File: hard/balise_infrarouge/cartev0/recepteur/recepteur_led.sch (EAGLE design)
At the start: 112 parts, among them IC2 7805DT, IC3 4051D, IC4 4051D, IC5 AT90CAN128A, J1 CAN, Q2 16M, X4 UART, X5 ISP

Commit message: maj emetteur + fini recepteur part 1
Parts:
- removed C27, C28, C29, C30, C4: 100n, rcl:C-EUC0805
- removed C3: 330n, rcl:C-EUC0805
- removed C31, C32: 22p, rcl:C-EUC0805
- removed D4: MBR130T1G, diode:DIODE-SOD123
- removed IC2: 7805DT, linear:7805DT
- removed IC5: AT90CAN128A, avr:AT90CAN128A
- removed J1: CAN, con-amp:557969-1
- removed LED2: CAN State, led:LEDCHIP-LED0805
- removed Q2: 16M, crystal:CRYSTALHC49UP
- removed R1: 0, rcl:R-EU_R0805
- removed R21: 0, rcl:R-EU_M0805
- removed R22, R25, R3: 10k, rcl:R-EU_R0805
- removed R24: 1k, rcl:R-EU_M0805
- removed X4: UART, con-molex:53261-04
- removed X5: ISP, con-molex:53261-06
- added SK2: (no value), jt-con-micromatch:MMATCH-10-PTH
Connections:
- removed net +12V: C3.1, D4.C, IC2.VI
- removed net CAN_CANH: J1.1
- removed net CAN_CANL: J1.2
- removed net CAN_RX: IC5.(RXCAN/T1)PD6
- removed net CAN_TX: IC5.(TXCAN/XCK1)PD5
- removed net ISP_PDO: IC5.(TXD0/PDO)PE1, X5-4.S
- removed net ISP_RST: C27.1, IC5.RESET, R22.1, X5-2.S
- removed net ISP_SCK: IC5.(SCK)PB1, X5-5.S
- removed net LED_CANSTATE: IC5.(OC1B)PB6, LED2.A
- removed net MUX0_INH: IC4A.INH, IC5.(XCK0/AIN0)PE2, R3.1
- removed net MUX1_INH: IC3A.INH, IC5.(AD6)PA6, R25.1
- removed net N$1: IC4A.X, R1.1
- removed net N$13: C32.1, IC5.XTAL1, Q2.2
- removed net N$14: C31.1, IC5.XTAL2, Q2.1
- removed net N$17: LED2.C, R24.2
- removed net N$34: D4.A, J1.4, J1.5
- removed net N$8: J1.8, R21.1
- removed net UART1_TX: IC5.(TXD1/INT3)PD3, X4-3.S
- net +5V: now also SK2.2; no longer C28.1, C29.1, C30.1, C4.1, IC2.VO, IC5.AREF, IC5.AVCC, IC5.VCC, IC5.VCC1, R21.2, R22.2, R25.2, R3.2, X4-1.S, X5-1.S
- net GND: now also IC3A.INH, IC4A.INH, SK2.1; no longer C27.2, C28.2, C29.2, C3.2, C30.2, C31.2, C32.2, C4.2, IC2.GND, IC5.AGND, IC5.GND, IC5.GND1, J1.3, J1.6, J1.7, J1.S1, J1.S2, R24.1, X4-4.S, X5-6.S
- net MUX0_A: now also SK2.10; no longer IC5.(OC3A/AIN1)PE3
- net MUX0_B: now also SK2.8; no longer IC5.(OC3B/INT4)PE4
- net MUX0_C: now also SK2.6; no longer IC5.(OC3C/INT5)PE5
- net MUX1_A: now also SK2.3; no longer IC5.(AD3)PA3
- net MUX1_B: now also SK2.5; no longer IC5.(AD4)PA4
- net MUX1_C: now also SK2.7; no longer IC5.(AD5)PA5
- net UART0_RX: now also IC4A.X, SK2.4; no longer IC5.(RXD0/PDI)PE0, R1.2, X5-3.S
- net UART1_RX: now also SK2.9; no longer IC5.(RXD1/INT2)PD2, X4-2.S
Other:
- note removed: "Interface CAN"

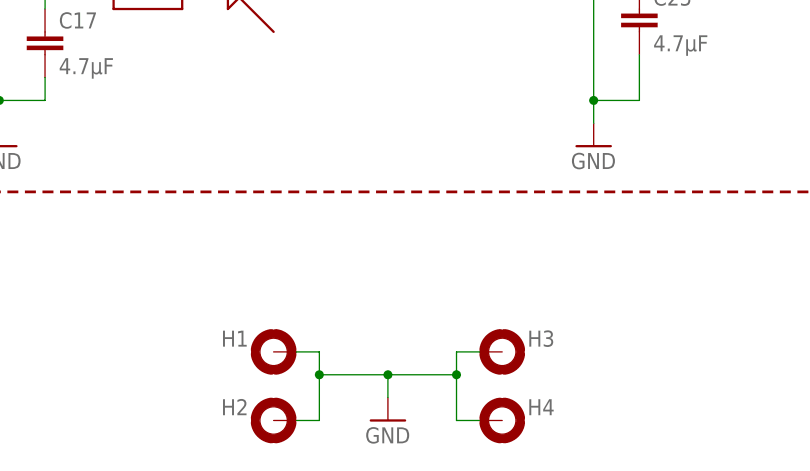
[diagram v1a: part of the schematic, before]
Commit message: maj carte extension nucleo
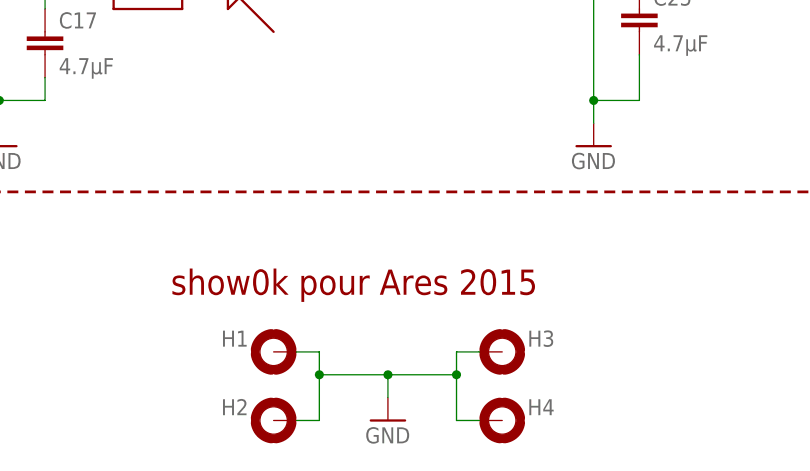
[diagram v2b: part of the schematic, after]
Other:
- note added: "show0k pour Ares 2015"
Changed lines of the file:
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@@
 <layer number="54" name="bGND_GNDA" color="1" fill="9" visible="no" active="no"/>
 <layer number="56" name="wert" color="7" fill="1" visible="no" active="no"/>
+<layer number="57" name="tCAD" color="7" fill="1" visible="no" active="no"/>
+<layer number="59" name="tCarbon" color="7" fill="1" visible="no" active="no"/>
+<layer number="60" name="bCarbon" color="7" fill="1" visible="no" active="no"/>
 <layer number="91" name="Nets" color="2" fill="1" visible="yes" active="yes"/>
 <layer number="92" name="Busses" color="1" fill="1" visible="yes" active="yes"/>
@@
 <layer number="101" name="Patch_Top" color="12" fill="4" visible="yes" active="yes"/>
 <layer number="102" name="Vscore" color="7" fill="1" visible="yes" active="yes"/>
+<layer number="103" name="tMap" color="7" fill="1" visible="yes" active="yes"/>
 <layer number="104" name="Name" color="7" fill="1" visible="yes" active="yes"/>
+<layer number="105" name="tPlate" color="7" fill="1" visible="yes" active="yes"/>
+<layer number="106" name="bPlate" color="7" fill="1" visible="yes" active="yes"/>
+<layer number="107" name="Crop" color="7" fill="1" visible="yes" active="yes"/>
+<layer number="108" name="fp8" color="7" fill="1" visible="yes" active="yes"/>
+<layer number="109" name="fp9" color="7" fill="1" visible="yes" active="yes"/>
+<layer number="110" name="fp0" color="7" fill="1" visible="yes" active="yes"/>
+<layer number="111" name="Design_Info" color="7" fill="1" visible="yes" active="yes"/>
+<layer number="112" name="CC430_Restrict" color="7" fill="1" visible="yes" active="yes"/>
 <layer number="116" name="Patch_BOT" color="9" fill="4" visible="yes" active="yes"/>
 <layer number="121" name="_tsilk" color="7" fill="1" visible="yes" active="yes"/>
 <layer number="122" name="_bsilk" color="7" fill="1" visible="yes" active="yes"/>
+<layer number="123" name="tTestmark" color="7" fill="1" visible="yes" active="yes"/>
+<layer number="124" name="bTestmark" color="7" fill="1" visible="yes" active="yes"/>
+<layer number="125" name="_tNames" color="7" fill="1" visible="yes" active="yes"/>
+<layer number="126" name="_bNames" color="7" fill="1" visible="yes" active="yes"/>
+<layer number="127" name="_tValues" color="7" fill="1" visible="yes" active="yes"/>
+<layer number="128" name="_bValues" color="7" fill="1" visible="yes" active="yes"/>
+<layer number="129" name="Mask" color="7" fill="1" visible="yes" active="yes"/>
+<layer number="131" name="tAdjust" color="7" fill="1" visible="yes" active="yes"/>
+<layer number="132" name="bAdjust" color="7" fill="1" visible="yes" active="yes"/>
+<layer number="144" name="Drill_legend" color="7" fill="1" visible="yes" active="yes"/>
+<layer number="150" name="Notes" color="7" fill="1" visible="no" active="yes"/>
 <layer number="151" name="HeatSink" color="7" fill="1" visible="yes" active="yes"/>
+<layer number="152" name="_bDocu" color="7" fill="1" visible="yes" active="yes"/>
+<layer number="153" name="FabDoc1" color="6" fill="1" visible="no" active="no"/>
+<layer number="154" name="FabDoc2" color="2" fill="1" visible="no" active="no"/>
+<layer number="155" name="FabDoc3" color="7" fill="15" visible="no" active="no"/>
+<layer number="199" name="Contour" color="7" fill="1" visible="yes" active="yes"/>
 <layer number="200" name="200bmp" color="1" fill="10" visible="no" active="no"/>
 <layer number="201" name="201bmp" color="2" fill="1" visible="no" active="no"/>
 <layer number="202" name="202bmp" color="3" fill="1" visible="no" active="no"/>
+<layer number="203" name="203bmp" color="4" fill="10" visible="yes" active="yes"/>
+<layer number="204" name="204bmp" color="5" fill="10" visible="yes" active="yes"/>
+<layer number="205" name="205bmp" color="6" fill="10" visible="yes" active="yes"/>
+<layer number="206" name="206bmp" color="7" fill="10" visible="yes" active="yes"/>
+<layer number="207" name="207bmp" color="8" fill="10" visible="yes" active="yes"/>
+<layer number="208" name="208bmp" color="9" fill="10" visible="yes" active="yes"/>
+<layer number="209" name="209bmp" color="7" fill="1" visible="yes" active="yes"/>
+<layer number="210" name="210bmp" color="7" fill="1" visible="yes" active="yes"/>
+<layer number="211" name="211bmp" color="7" fill="1" visible="yes" active="yes"/>
+<layer number="212" name="212bmp" color="7" fill="1" visible="yes" active="yes"/>
+<layer number="213" name="213bmp" color="7" fill="1" visible="yes" active="yes"/>
+<layer number="214" name="214bmp" color="7" fill="1" visible="yes" active="yes"/>
+<layer number="215" name="215bmp" color="7" fill="1" visible="yes" active="yes"/>
+<layer number="216" name="216bmp" color="7" fill="1" visible="yes" active="yes"/>
+<layer number="217" name="217bmp" color="18" fill="1" visible="no" active="no"/>
+<layer number="218" name="218bmp" color="19" fill="1" visible="no" active="no"/>
+<layer number="219" name="219bmp" color="20" fill="1" visible="no" active="no"/>
+<layer number="220" name="220bmp" color="21" fill="1" visible="no" active="no"/>
+<layer number="221" name="221bmp" color="22" fill="1" visible="no" active="no"/>
+<layer number="222" name="222bmp" color="23" fill="1" visible="no" active="no"/>
+<layer number="223" name="223bmp" color="24" fill="1" visible="no" active="no"/>
+<layer number="224" name="224bmp" color="25" fill="1" visible="no" active="no"/>
+<layer number="248" name="Housing" color="7" fill="1" visible="yes" active="yes"/>
+<layer number="249" name="Edge" color="7" fill="1" visible="yes" active="yes"/>
 <layer number="250" name="Descript" color="3" fill="1" visible="no" active="no"/>
 <layer number="251" name="SMDround" color="12" fill="11" visible="no" active="no"/>
@@
 <text x="12.7" y="101.6" size="2.54" layer="94">Multiplexage sériel</text>
 <text x="238.76" y="246.38" size="2.54" layer="94">Récepteurs IR 455kHz</text>
+<text x="290.83" y="24.13" size="2.794" layer="94" font="vector" ratio="14">show0k pour Ares 2015</text>
 </plain>
 <instances>
